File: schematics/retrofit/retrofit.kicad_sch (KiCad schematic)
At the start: 0 parts

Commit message: schematics
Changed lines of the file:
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@@
 (kicad_sch (version 20230121) (generator eeschema)
   (paper "A4")
-  (sheet (at 186.69 69.85) (size 35.56 15.24) (fields_autoplaced)
+  (sheet (at 167.64 73.66) (size 35.56 15.24) (fields_autoplaced)
     (stroke (width 0.1524) (type solid))
     (fill (color 0 0 0 0.0000))
-    (property "Sheetname" "PWR" (at 186.69 69.1384 0)
+    (property "Sheetname" "PWR" (at 167.64 72.9484 0)
       (effects (font (size 1.27 1.27)) (justify left bottom))
     )
-    (property "Sheetfile" "PWR.kicad_sch" (at 186.69 85.6746 0)
+    (property "Sheetfile" "PWR.kicad_sch" (at 167.64 89.4846 0)
       (effects (font (size 1.27 1.27)) (justify left top))
     )
@@
     )
   )
-  (sheet (at 144.78 69.85) (size 34.29 15.24) (fields_autoplaced)
+  (sheet (at 125.73 73.66) (size 34.29 15.24) (fields_autoplaced)
     (stroke (width 0.1524) (type solid))
     (fill (color 0 0 0 0.0000))
-    (property "Sheetname" "MAHO Inputs" (at 144.78 69.1384 0)
+    (property "Sheetname" "MAHO Inputs" (at 125.73 72.9484 0)
       (effects (font (size 1.27 1.27)) (justify left bottom))
     )
-    (property "Sheetfile" "MAHO_Inputs.kicad_sch" (at 144.78 85.6746 0)
+    (property "Sheetfile" "MAHO_Inputs.kicad_sch" (at 125.73 89.4846 0)
       (effects (font (size 1.27 1.27)) (justify left top))
     )
@@
     )
   )
-  (sheet (at 104.14 95.25) (size 34.29 15.24) (fields_autoplaced)
+  (sheet (at 85.09 99.06) (size 34.29 15.24) (fields_autoplaced)
     (stroke (width 0.1524) (type solid))
     (fill (color 0 0 0 0.0000))
-    (property "Sheetname" "Servos" (at 104.14 94.5384 0)
+    (property "Sheetname" "Servos" (at 85.09 98.3484 0)
       (effects (font (size 1.27 1.27)) (justify left bottom))
     )
-    (property "Sheetfile" "Servos.kicad_sch" (at 104.14 111.0746 0)
+    (property "Sheetfile" "Servos.kicad_sch" (at 85.09 114.8846 0)
       (effects (font (size 1.27 1.27)) (justify left top))
     )
@@
     )
   )
-  (sheet (at 186.69 95.25) (size 35.56 15.24) (fields_autoplaced)
+  (sheet (at 167.64 99.06) (size 35.56 15.24) (fields_autoplaced)
     (stroke (width 0.1524) (type solid))
     (fill (color 0 0 0 0.0000))
-    (property "Sheetname" "RS485" (at 186.69 94.5384 0)
+    (property "Sheetname" "RS485" (at 167.64 98.3484 0)
       (effects (font (size 1.27 1.27)) (justify left bottom))
     )
-    (property "Sheetfile" "RS485.kicad_sch" (at 186.69 111.0746 0)
+    (property "Sheetfile" "RS485.kicad_sch" (at 167.64 114.8846 0)
       (effects (font (size 1.27 1.27)) (justify left top))
     )
@@
     )
   )
-  (sheet (at 144.78 95.25) (size 34.29 15.24) (fields_autoplaced)
+  (sheet (at 125.73 99.06) (size 34.29 15.24) (fields_autoplaced)
     (stroke (width 0.1524) (type solid))
     (fill (color 0 0 0 0.0000))
-    (property "Sheetname" "MAHO Outputs" (at 144.78 94.5384 0)
+    (property "Sheetname" "MAHO Outputs" (at 125.73 98.3484 0)
       (effects (font (size 1.27 1.27)) (justify left bottom))
     )
-    (property "Sheetfile" "MAHO_Outputs.kicad_sch" (at 144.78 111.0746 0)
+    (property "Sheetfile" "MAHO_Outputs.kicad_sch" (at 125.73 114.8846 0)
       (effects (font (size 1.27 1.27)) (justify left top))
     )
@@
     )
   )
-  (sheet (at 104.14 69.85) (size 34.29 15.24) (fields_autoplaced)
+  (sheet (at 85.09 73.66) (size 34.29 15.24) (fields_autoplaced)
     (stroke (width 0.1524) (type solid))
     (fill (color 0 0 0 0.0000))
-    (property "Sheetname" "Encoders" (at 104.14 69.1384 0)
+    (property "Sheetname" "Encoders" (at 85.09 72.9484 0)
       (effects (font (size 1.27 1.27)) (justify left bottom))
     )
-    (property "Sheetfile" "Encoders.kicad_sch" (at 104.14 85.6746 0)
+    (property "Sheetfile" "Encoders.kicad_sch" (at 85.09 89.4846 0)
       (effects (font (size 1.27 1.27)) (justify left top))
     )

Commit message: draft
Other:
- sheet MAHO Inputs renamed MAHO Inputs -  Mesa Outputs
- sheet MAHO Outputs renamed MAHO Outputs - MESA Inputs
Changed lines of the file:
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@@
     (stroke (width 0.1524) (type solid))
     (fill (color 0 0 0 0.0000))
-    (property "Sheetname" "MAHO Inputs" (at 125.73 72.9484 0)
+    (property "Sheetname" "MAHO Inputs -  Mesa Outputs" (at 125.73 72.9484 0)
       (effects (font (size 1.27 1.27)) (justify left bottom))
     )
@@
     (stroke (width 0.1524) (type solid))
     (fill (color 0 0 0 0.0000))
-    (property "Sheetname" "MAHO Outputs" (at 125.73 98.3484 0)
+    (property "Sheetname" "MAHO Outputs - MESA Inputs" (at 125.73 98.3484 0)
       (effects (font (size 1.27 1.27)) (justify left bottom))
     )

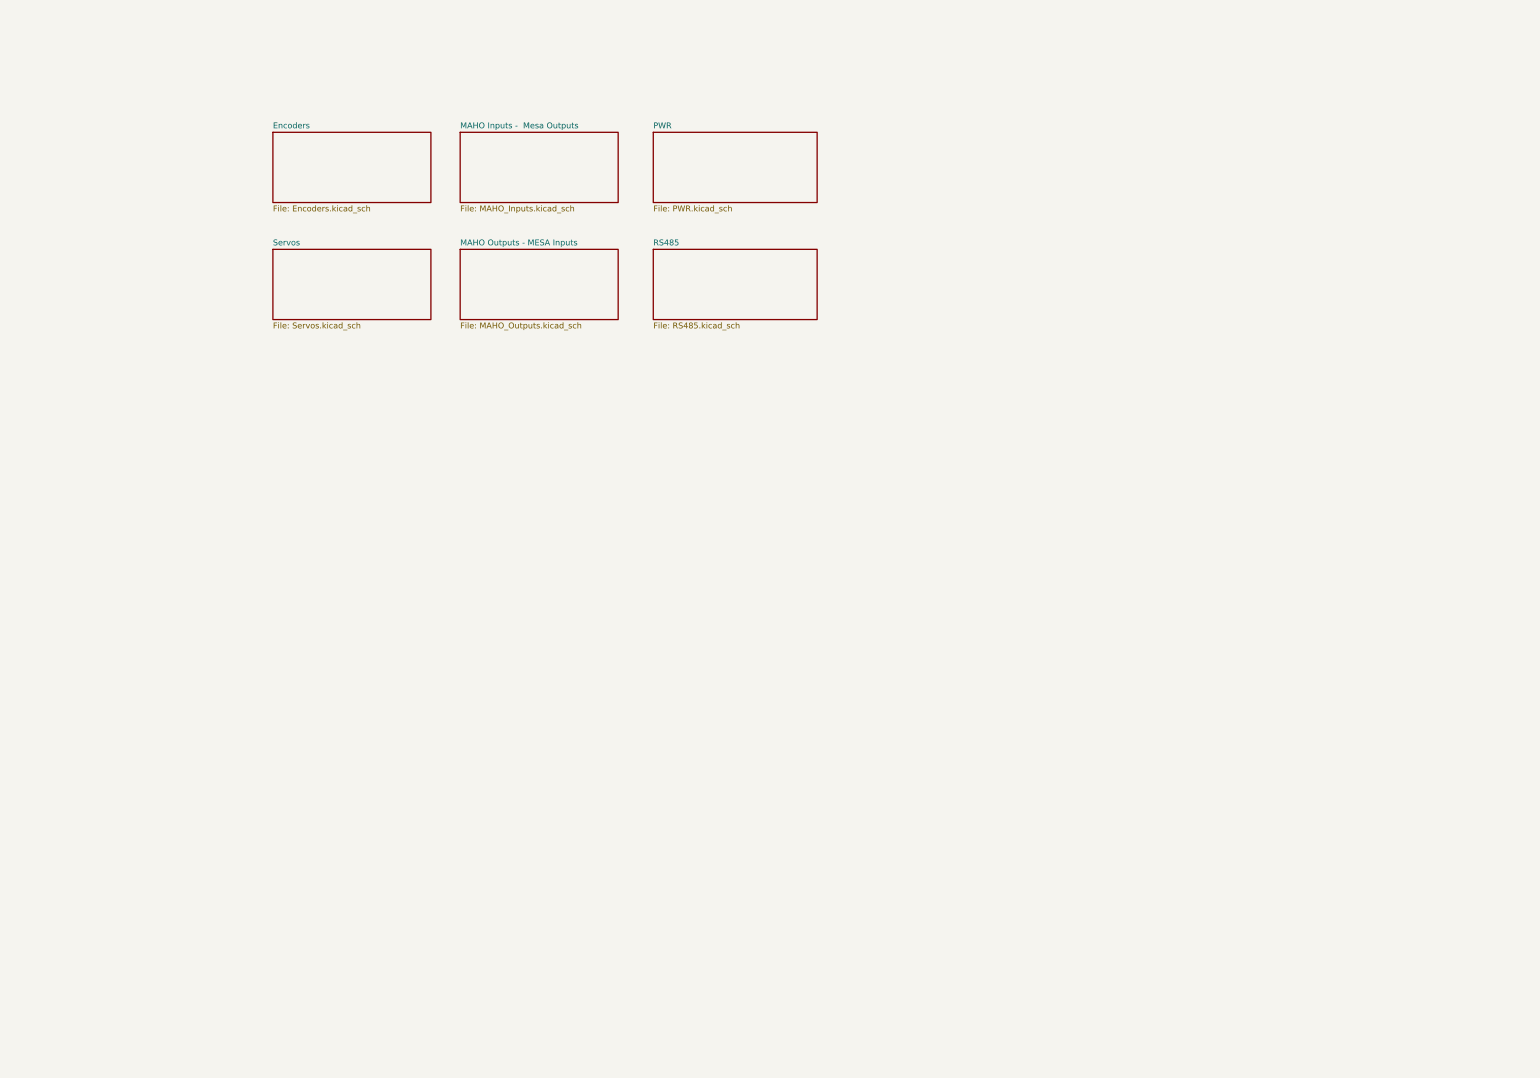
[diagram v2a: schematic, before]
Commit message: maho-io component and english manual
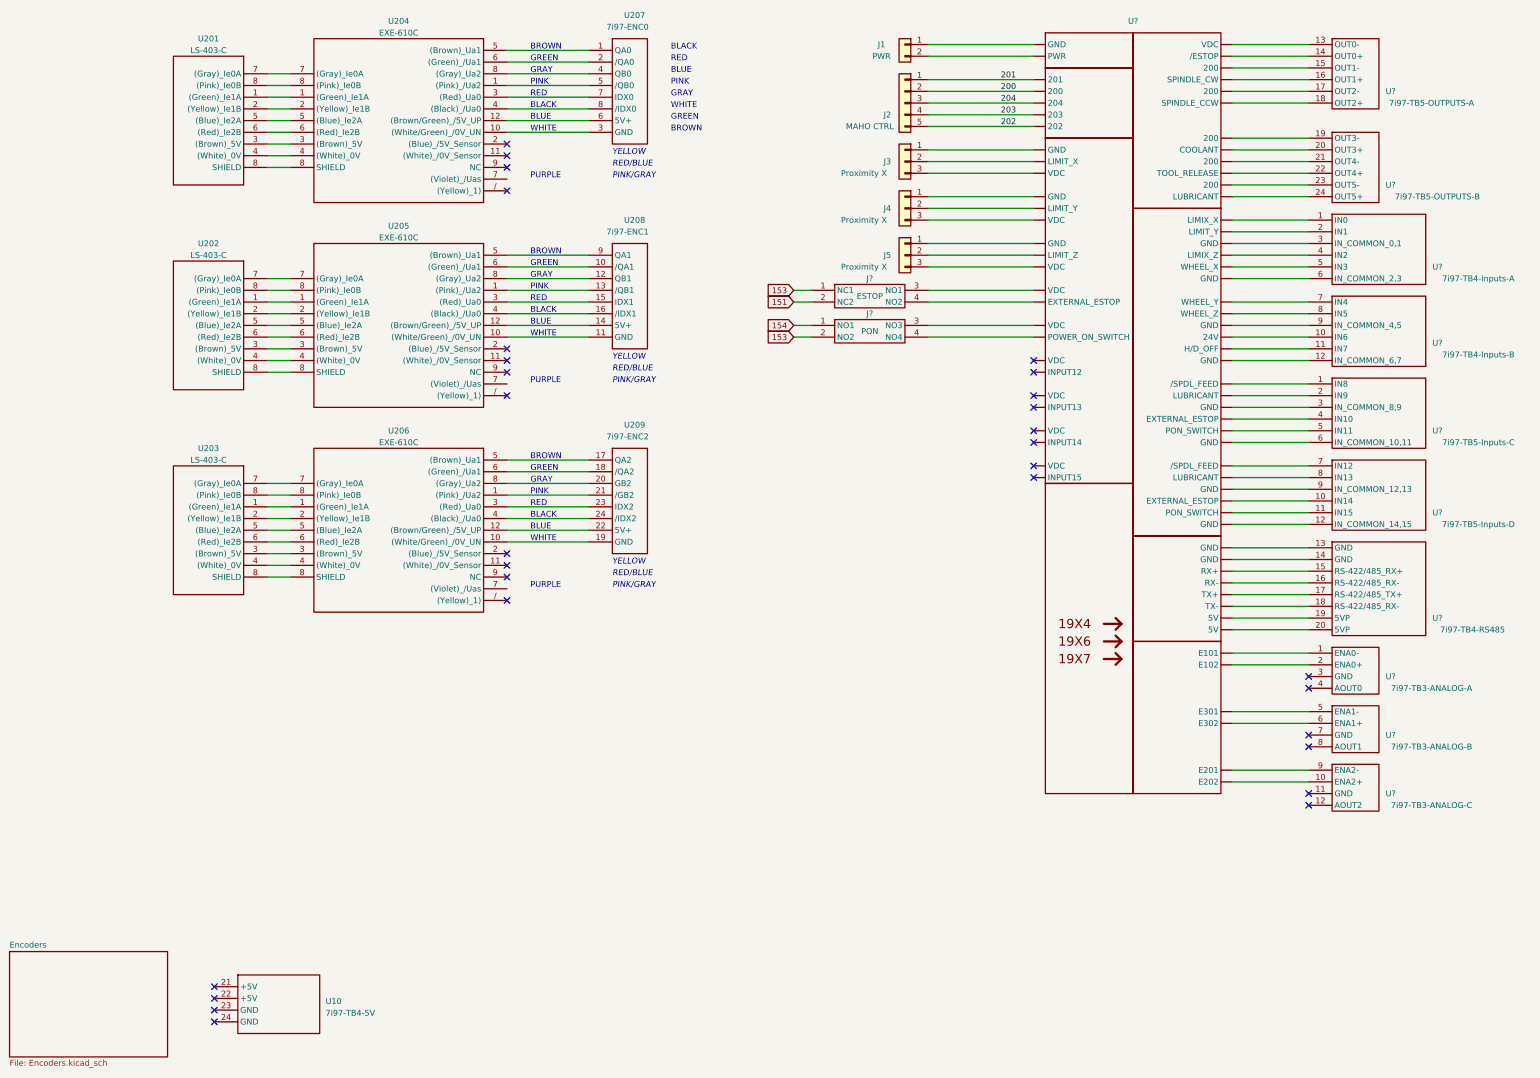
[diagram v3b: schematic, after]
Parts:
- added J1: PWR, symbol Connector_Generic:Conn_01x02
- added J2: MAHO CTRL, symbol Connector_Generic:Conn_01x05
- added J3, J4, J5: Proximity X, symbol Connector_Generic:Conn_01x03
- added J?: ESTOP, symbol MAHO:ESTOP
- added J?: PON, symbol MAHO:PWR_SWITCH
- added U10: 7i97-TB4-5V, symbol MAHO:7i97-TB4-5V
- added U201, U202, U203: LS-403-C, symbol MAHO:LS-403-C
- added U204, U205, U206: EXE-610C, symbol MAHO:EXE-610C
- added U207: 7i97-ENC0, symbol MAHO:7i97-ENC0
- added U208: 7i97-ENC1, symbol MAHO:7i97-ENC1
- added U209: 7i97-ENC2, symbol MAHO:7i97-ENC2
- added U?: 7i97-TB3-ANALOG-C, symbol MAHO:7i97-TB3-ANALOG-C
- added U?: (no value), symbol MAHO:Breakout
- added U?: 7i97-TB3-ANALOG-A, symbol MAHO:7i97-TB3-ANALOG-A
- added U?: 7i97-TB3-ANALOG-B, symbol MAHO:7i97-TB3-ANALOG-B
- added U?: 7i97-TB4-Inputs-B, symbol MAHO:7i97-TB4-Inputs-B
- added U?: 7i97-TB5-OUTPUTS-A, symbol MAHO:7i97-TB5-OUTPUTS-A
- added U?: 7i97-TB5-Inputs-D, symbol MAHO:7i97-TB5-Inputs-D
- added U?: 7i97-TB4-Inputs-A, symbol MAHO:7i97-TB4-Inputs-A
- added U?: 7i97-TB4-RS485, symbol MAHO:7i97-TB4-RS485
- added U?: 7i97-TB5-Inputs-C, symbol MAHO:7i97-TB5-Inputs-C
- added U?: 7i97-TB5-OUTPUTS-B, symbol MAHO:7i97-TB5-OUTPUTS-B
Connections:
- new net: U203.1 ((Green)_Ie1A), U206.1 ((Pink)_/Ua2)
- new net: U206.1 ((Pink)_/Ua2), U209.21 (/GB2)
- new net: U206.10 ((White/Green)_/0V_UN), U209.19 (GND)
- new net: U206.12 ((Brown/Green)_/5V_UP), U209.22 (5V+)
- new net: U203.2 ((Yellow)_Ie1B), U206.2 ((Yellow)_Ie1B)
- new net: U203.3 ((Brown)_5V), U206.3 ((Red)_Ua0)
- new net: U206.3 ((Red)_Ua0), U209.23 (IDX2)
- new net: U203.4 ((White)_0V), U206.4 ((White)_0V)
- new net: U206.4 ((White)_0V), U209.24 (/IDX2)
- new net: U203.5 ((Blue)_Ie2A), U206.5 ((Brown)_Ua1)
- new net: U206.5 ((Brown)_Ua1), U209.17 (QA2)
- new net: U203.6 ((Red)_Ie2B), U206.6 ((Red)_Ie2B)
- new net: U206.6 ((Red)_Ie2B), U209.18 (/QA2)
- new net: U203.7 ((Gray)_Ie0A), U206.7 ((Violet)_/Uas)
- new net: U203.8 (SHIELD), U206.8 (SHIELD) (x2)
- new net: U206.8 (SHIELD), U209.20 (GB2)
- new net: U204.1 ((Pink)_/Ua2), U207.5 (/QB0)
- new net: U201.1 ((Green)_Ie1A), U204.1 ((Pink)_/Ua2)
- new net: U204.10 ((White/Green)_/0V_UN), U207.3 (GND)
- new net: U204.12 ((Brown/Green)_/5V_UP), U207.6 (5V+)
- new net: U201.2 ((Yellow)_Ie1B), U204.2 ((Yellow)_Ie1B)
- new net: U204.3 ((Red)_Ua0), U207.7 (IDX0)
- new net: U201.3 ((Brown)_5V), U204.3 ((Red)_Ua0)
- new net: U204.4 ((White)_0V), U207.8 (/IDX0)
- new net: U201.4 ((White)_0V), U204.4 ((White)_0V)
- new net: U204.5 ((Brown)_Ua1), U207.1 (QA0)
- new net: U201.5 ((Blue)_Ie2A), U204.5 ((Brown)_Ua1)
- new net: U204.6 ((Red)_Ie2B), U207.2 (/QA0)
- new net: U201.6 ((Red)_Ie2B), U204.6 ((Red)_Ie2B)
- new net: U201.7 ((Gray)_Ie0A), U204.7 ((Violet)_/Uas)
- new net: U204.8 (SHIELD), U207.4 (QB0)
- new net: U201.8 (SHIELD), U204.8 (SHIELD) (x2)
- new net: U205.6 ((Red)_Ie2B), U208.10 (/QA1)
- new net: U205.10 ((White/Green)_/0V_UN), U208.11 (GND)
- new net: U205.8 (SHIELD), U208.12 (QB1)
- new net: U205.1 ((Pink)_/Ua2), U208.13 (/QB1)
- new net: U205.12 ((Brown/Green)_/5V_UP), U208.14 (5V+)
- new net: U205.3 ((Red)_Ua0), U208.15 (IDX1)
- new net: U205.4 ((White)_0V), U208.16 (/IDX1)
- new net: U205.5 ((Brown)_Ua1), U208.9 (QA1)
- new net: U?. (WHEEL_Z), U?.10 (ENA2+)
- new net: U?. (WHEEL_Z), U?.9 (ENA2-)
- new net: U202.1 ((Green)_Ie1A), U205.1 ((Pink)_/Ua2)
- new net: U202.2 ((Yellow)_Ie1B), U205.2 ((Yellow)_Ie1B)
- new net: U202.3 ((Brown)_5V), U205.3 ((Red)_Ua0)
- new net: U202.4 ((White)_0V), U205.4 ((White)_0V)
- new net: U202.5 ((Blue)_Ie2A), U205.5 ((Brown)_Ua1)
- new net: U202.6 ((Red)_Ie2B), U205.6 ((Red)_Ie2B)
- new net: U202.7 ((Gray)_Ie0A), U205.7 ((Violet)_/Uas)
- new net: U202.8 (SHIELD), U205.8 (SHIELD) (x2)
- new net: J4.1 (Pin_1), U?. (WHEEL_Z)
- new net: J4.2 (Pin_2), U?. (WHEEL_Z)
- new net: J4.3 (Pin_3), U?. (WHEEL_Z)
- new net: J1.1 (Pin_1), U?. (WHEEL_Z)
- new net: J1.2 (Pin_2), U?. (WHEEL_Z)
- new net: J?.3 (NO1), U?. (WHEEL_Z)
- new net: J?.4 (NO2), U?. (WHEEL_Z)
- new net: U?. (WHEEL_Z), U?.1 (ENA0-)
- new net: U?. (WHEEL_Z), U?.2 (ENA0+)
- new net: U?. (WHEEL_Z), U?.5 (ENA1-)
- new net: U?. (WHEEL_Z), U?.6 (ENA1+)
- new net: U?. (WHEEL_Z), U?.10 (IN6)
- new net: U?. (WHEEL_Z), U?.11 (IN7)
- new net: U?. (WHEEL_Z), U?.12 (IN_COMMON_6,7)
- new net: U?. (WHEEL_Z), U?.7 (IN4)
- new net: U?. (WHEEL_Z), U?.8 (IN5)
- new net: U?. (WHEEL_Z), U?.9 (IN_COMMON_4,5)
- new net: J5.1 (Pin_1), U?. (WHEEL_Z)
- new net: J5.2 (Pin_2), U?. (WHEEL_Z)
- new net: J5.3 (Pin_3), U?. (WHEEL_Z)
- new net: U?. (WHEEL_Z), U?.13 (OUT0-)
- new net: U?. (WHEEL_Z), U?.14 (OUT0+)
- new net: U?. (WHEEL_Z), U?.15 (OUT1-)
- new net: U?. (WHEEL_Z), U?.16 (OUT1+)
- new net: U?. (WHEEL_Z), U?.17 (OUT2-)
- new net: U?. (WHEEL_Z), U?.18 (OUT2+)
- new net: U?. (WHEEL_Z), U?.10 (IN14)
- new net: U?. (WHEEL_Z), U?.11 (IN15)
- new net: U?. (WHEEL_Z), U?.12 (IN_COMMON_14,15)
- new net: U?. (WHEEL_Z), U?.7 (IN12)
- new net: U?. (WHEEL_Z), U?.8 (IN13)
- new net: U?. (WHEEL_Z), U?.9 (IN_COMMON_12,13)
- new net: U?. (WHEEL_Z), U?.1 (IN0)
- new net: U?. (WHEEL_Z), U?.2 (IN1)
- new net: U?. (WHEEL_Z), U?.3 (IN_COMMON_0,1)
- new net: U?. (WHEEL_Z), U?.4 (IN2)
- new net: U?. (WHEEL_Z), U?.5 (IN3)
- new net: U?. (WHEEL_Z), U?.6 (IN_COMMON_2,3)
- new net: U?. (WHEEL_Z), U?.13 (GND)
- new net: U?. (WHEEL_Z), U?.14 (GND)
- new net: U?. (WHEEL_Z), U?.15 (RS-422/485_RX+)
- new net: U?. (WHEEL_Z), U?.16 (RS-422/485_RX-)
- new net: U?. (WHEEL_Z), U?.17 (RS-422/485_TX+)
- new net: U?. (WHEEL_Z), U?.18 (RS-422/485_RX-)
- new net: U?. (WHEEL_Z), U?.19 (5VP)
- new net: U?. (WHEEL_Z), U?.20 (5VP)
- new net: U?. (WHEEL_Z), U?.1 (IN8)
- new net: U?. (WHEEL_Z), U?.2 (IN9)
- new net: U?. (WHEEL_Z), U?.3 (IN_COMMON_8,9)
- new net: U?. (WHEEL_Z), U?.4 (IN10)
- new net: U?. (WHEEL_Z), U?.5 (IN11)
- new net: U?. (WHEEL_Z), U?.6 (IN_COMMON_10,11)
- new net: U?. (WHEEL_Z), U?.19 (OUT3-)
- new net: U?. (WHEEL_Z), U?.20 (OUT3+)
- new net: U?. (WHEEL_Z), U?.21 (OUT4-)
- new net: U?. (WHEEL_Z), U?.22 (OUT4+)
- new net: U?. (WHEEL_Z), U?.23 (OUT5-)
- new net: U?. (WHEEL_Z), U?.24 (OUT5+)
- new net: J?.3 (NO3), U?. (WHEEL_Z)
- new net: J?.4 (NO4), U?. (WHEEL_Z)
- new net: J3.1 (Pin_1), U?. (WHEEL_Z)
- new net: J3.2 (Pin_2), U?. (WHEEL_Z)
- new net: J3.3 (Pin_3), U?. (WHEEL_Z)
- new net 151: J?.2 (NC2)
- new net 153: J?.1 (NC1), J?.2 (NO2)
- new net 154: J?.1 (NO1)
- new net 200: J2.2 (Pin_2), U?. (WHEEL_Z)
- new net 201: J2.1 (Pin_1), U?. (WHEEL_Z)
- new net 202: J2.5 (Pin_5), U?. (WHEEL_Z)
- new net 203: J2.4 (Pin_4), U?. (WHEEL_Z)
- new net 204: J2.3 (Pin_3), U?. (WHEEL_Z)
- no-connect marks 0 -> 30
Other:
- removed sheet MAHO Inputs -  Mesa Outputs
- removed sheet MAHO Outputs - MESA Inputs
- removed sheet PWR
- removed sheet RS485
- removed sheet Servos
- note added: "BLACK"
- note added: "BLUE"
- note added: "BROWN"
- note added: "GRAY"
- note added: "GREEN"
- note added: "PINK"
- note added: "PINK/GRAY"
- note added: "PURPLE"
- note added: "RED"
- note added: "RED/BLUE"
- note added: "WHITE"
- note added: "YELLOW"

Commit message: sch
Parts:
- removed U?: 7i97-TB3-ANALOG-C, symbol MAHO:7i97-TB3-ANALOG-C
- removed U?: 7i97-TB3-ANALOG-A, symbol MAHO:7i97-TB3-ANALOG-A
- removed U?: 7i97-TB3-ANALOG-B, symbol MAHO:7i97-TB3-ANALOG-B
- removed U?: 7i97-TB4-Inputs-B, symbol MAHO:7i97-TB4-Inputs-B
- removed U?: 7i97-TB5-Inputs-D, symbol MAHO:7i97-TB5-Inputs-D
- removed U?: 7i97-TB4-Inputs-A, symbol MAHO:7i97-TB4-Inputs-A
- removed U?: 7i97-TB4-RS485, symbol MAHO:7i97-TB4-RS485
- removed U?: 7i97-TB5-Inputs-C, symbol MAHO:7i97-TB5-Inputs-C
- removed U?: 7i97-TB5-OUTPUTS-B, symbol MAHO:7i97-TB5-OUTPUTS-B
- added U10: 7i97-TB5-Inputs-D, symbol MAHO:7i97-TB5-Inputs-D
- added U11: 7i97-TB4-Inputs-A, symbol MAHO:7i97-TB4-Inputs-A
- added U2: 7i97-TB4-RS485, symbol MAHO:7i97-TB4-RS485
- added U3: 7i97-TB3-ANALOG-A, symbol MAHO:7i97-TB3-ANALOG-A
- added U5: 7i97-TB3-ANALOG-B, symbol MAHO:7i97-TB3-ANALOG-B
- added U6: 7i97-TB3-ANALOG-C, symbol MAHO:7i97-TB3-ANALOG-C
- added U8: 7i97-TB4-Inputs-B, symbol MAHO:7i97-TB4-Inputs-B
- added U9: 7i97-TB5-Inputs-C, symbol MAHO:7i97-TB5-Inputs-C
- added U?: 19Χ4, symbol MAHO:19Χ4
- added U?: 7i97-TB5-OUTPUTS-B, symbol MAHO:7i97-TB5-OUTPUTS-B
- added U?: 19X6, symbol MAHO:19X6
- added U?: 19X7, symbol MAHO:19X7
- gave numbers to parts that had none: 1
- renumbered U10 to U?
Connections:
- net 153: now also J?.1 (NO1); no longer J?.2 (NO2)
- net 154: now also J?.2 (NO2); no longer J?.1 (NO1)
- net at U206.2 ((Yellow)_Ie1B): now also U203.2 ((Yellow)_Ie1B)
- net at U206.7 ((Violet)_/Uas): now also U203.7 ((Gray)_Ie0A)
- net at U206.8 (SHIELD): now also U209.20 (GB2); no longer U203.8 (SHIELD)
- net at U204.2 ((Yellow)_Ie1B): now also U201.2 ((Yellow)_Ie1B)
- net at U204.7 ((Violet)_/Uas): now also U201.7 ((Gray)_Ie0A)
- new net: B?. (WHEEL_Z), U?.19Χ4-1 ((Brown)_E101)
- new net: B?. (WHEEL_Z), U?.19Χ4-2 ((Blue)_E102)
- new net: B?. (WHEEL_Z), U?.19Χ4-3 ((White)_E201)
- new net: B?. (WHEEL_Z), U?.19Χ4-4 ((Brown)_E202)
- new net: B?. (WHEEL_Z), U?.19Χ4-5 ((Yellow)_E301)
- new net: B?. (WHEEL_Z), U?.19Χ4-9 ((Pink)_E302)
- new net: B?. (WHEEL_Z), U2.13 (GND)
- new net: B?. (WHEEL_Z), U2.14 (GND)
- new net: B?. (WHEEL_Z), U2.15 (RS-422/485_RX+)
- new net: B?. (WHEEL_Z), U2.16 (RS-422/485_RX-)
- new net: B?. (WHEEL_Z), U2.17 (RS-422/485_TX+)
- new net: B?. (WHEEL_Z), U2.18 (RS-422/485_RX-)
- new net: B?. (WHEEL_Z), U2.19 (5VP)
- new net: B?. (WHEEL_Z), U2.20 (5VP)
- new net: U203.8 (SHIELD), U206.8 (SHIELD)
- new net: U201.8 (SHIELD), U204.8 (SHIELD)
- new net: U202.8 (SHIELD), U205.8 (SHIELD)
- new net: B?. (WHEEL_Z), U6.10 (ENA2+)
- new net: B?. (WHEEL_Z), U6.9 (ENA2-)
- new net: B?. (WHEEL_Z), U?.19 (OUT3-)
- new net: B?. (WHEEL_Z), U?.20 (OUT3+)
- new net: B?. (WHEEL_Z), U?.21 (OUT4-)
- new net: B?. (WHEEL_Z), U?.22 (OUT4+)
- new net: B?. (WHEEL_Z), U?.23 (OUT5-)
- new net: B?. (WHEEL_Z), U?.24 (OUT5+)
- new net: B?. (WHEEL_Z), U11.1 (IN0)
- new net: B?. (WHEEL_Z), U11.2 (IN1)
- new net: B?. (WHEEL_Z), U11.3 (IN_COMMON_0,1)
- new net: B?. (WHEEL_Z), U11.4 (IN2)
- new net: B?. (WHEEL_Z), U11.5 (IN3)
- new net: B?. (WHEEL_Z), U11.6 (IN_COMMON_2,3)
- new net: B?. (WHEEL_Z), U?.19X6-1 ((White)_X_Axis_Wheel)
- new net: B?. (WHEEL_Z), U?.19X6-2 ((Brown)_Y_Axis_Wheel)
- new net: B?. (WHEEL_Z), U?.19X6-3 ((Green)_Z_Axis_Wheel)
- new net: B?. (WHEEL_Z), U?.19X6-34 ((sw)_/ESTOP)
- new net: B?. (WHEEL_Z), U?.19X6-4 ((Yellow)_Spindle_CW)
- new net: B?. (WHEEL_Z), U?.19X6-5 ((Gray)_Spindle_CCW)
- new net: B?. (WHEEL_Z), U?.19X6-6 ((Pink)_Coolant_Pump)
- new net: B?. (WHEEL_Z), U?.19X6-7 ((Blue)_Tool_Release)
- new net: B?. (WHEEL_Z), U?.19X6-8 ((Red)_Central_Lubrication)
- new net: B?. (WHEEL_Z), U10.10 (IN14)
- new net: B?. (WHEEL_Z), U10.11 (IN15)
- new net: B?. (WHEEL_Z), U10.12 (IN_COMMON_14,15)
- new net: B?. (WHEEL_Z), U10.7 (IN12)
- new net: B?. (WHEEL_Z), U10.8 (IN13)
- new net: B?. (WHEEL_Z), U10.9 (IN_COMMON_12,13)
- new net: B?. (WHEEL_Z), U5.5 (ENA1-)
- new net: B?. (WHEEL_Z), U5.6 (ENA1+)
- new net: B?. (WHEEL_Z), U?.19X7-1 ((White)_Handwheel-X)
- new net: B?. (WHEEL_Z), U?.19X7-2 ((Brown)_Handwheel-Y)
- new net: B?. (WHEEL_Z), U?.19X7-3 ((Green)_Handwheel-Z)
- new net: B?. (WHEEL_Z), U?.19X7-4 ((Yellow)_24V)
- new net: B?. (WHEEL_Z), U?.19X7-5 ((Gray)_Spindle_OFF)
- new net: B?. (WHEEL_Z), U?.19X7-6 ((Pink)_/_Spindle_Feed_Stop)
- new net: B?. (WHEEL_Z), U?.19X7-7 ((Blue)_Pump_Feedback)
- new net: B?. (WHEEL_Z), U3.1 (ENA0-)
- new net: B?. (WHEEL_Z), U3.2 (ENA0+)
- new net: B?. (WHEEL_Z), U8.10 (IN6)
- new net: B?. (WHEEL_Z), U8.11 (IN7)
- new net: B?. (WHEEL_Z), U8.12 (IN_COMMON_6,7)
- new net: B?. (WHEEL_Z), U8.7 (IN4)
- new net: B?. (WHEEL_Z), U8.8 (IN5)
- new net: B?. (WHEEL_Z), U8.9 (IN_COMMON_4,5)
- new net: B?. (WHEEL_Z), U9.1 (IN8)
- new net: B?. (WHEEL_Z), U9.2 (IN9)
- new net: B?. (WHEEL_Z), U9.3 (IN_COMMON_8,9)
- new net: B?. (WHEEL_Z), U9.4 (IN10)
- new net: B?. (WHEEL_Z), U9.5 (IN11)
- new net: B?. (WHEEL_Z), U9.6 (IN_COMMON_10,11)
- no-connect marks 30 -> 36
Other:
- moved on the sheet: J1, J2, J3, J4, J5, J?, U201, U202, U203, U204, U205, U206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
